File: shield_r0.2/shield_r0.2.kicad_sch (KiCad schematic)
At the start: 10 parts, among them X6 X6, X7 X7, X8 X8, X9 X9

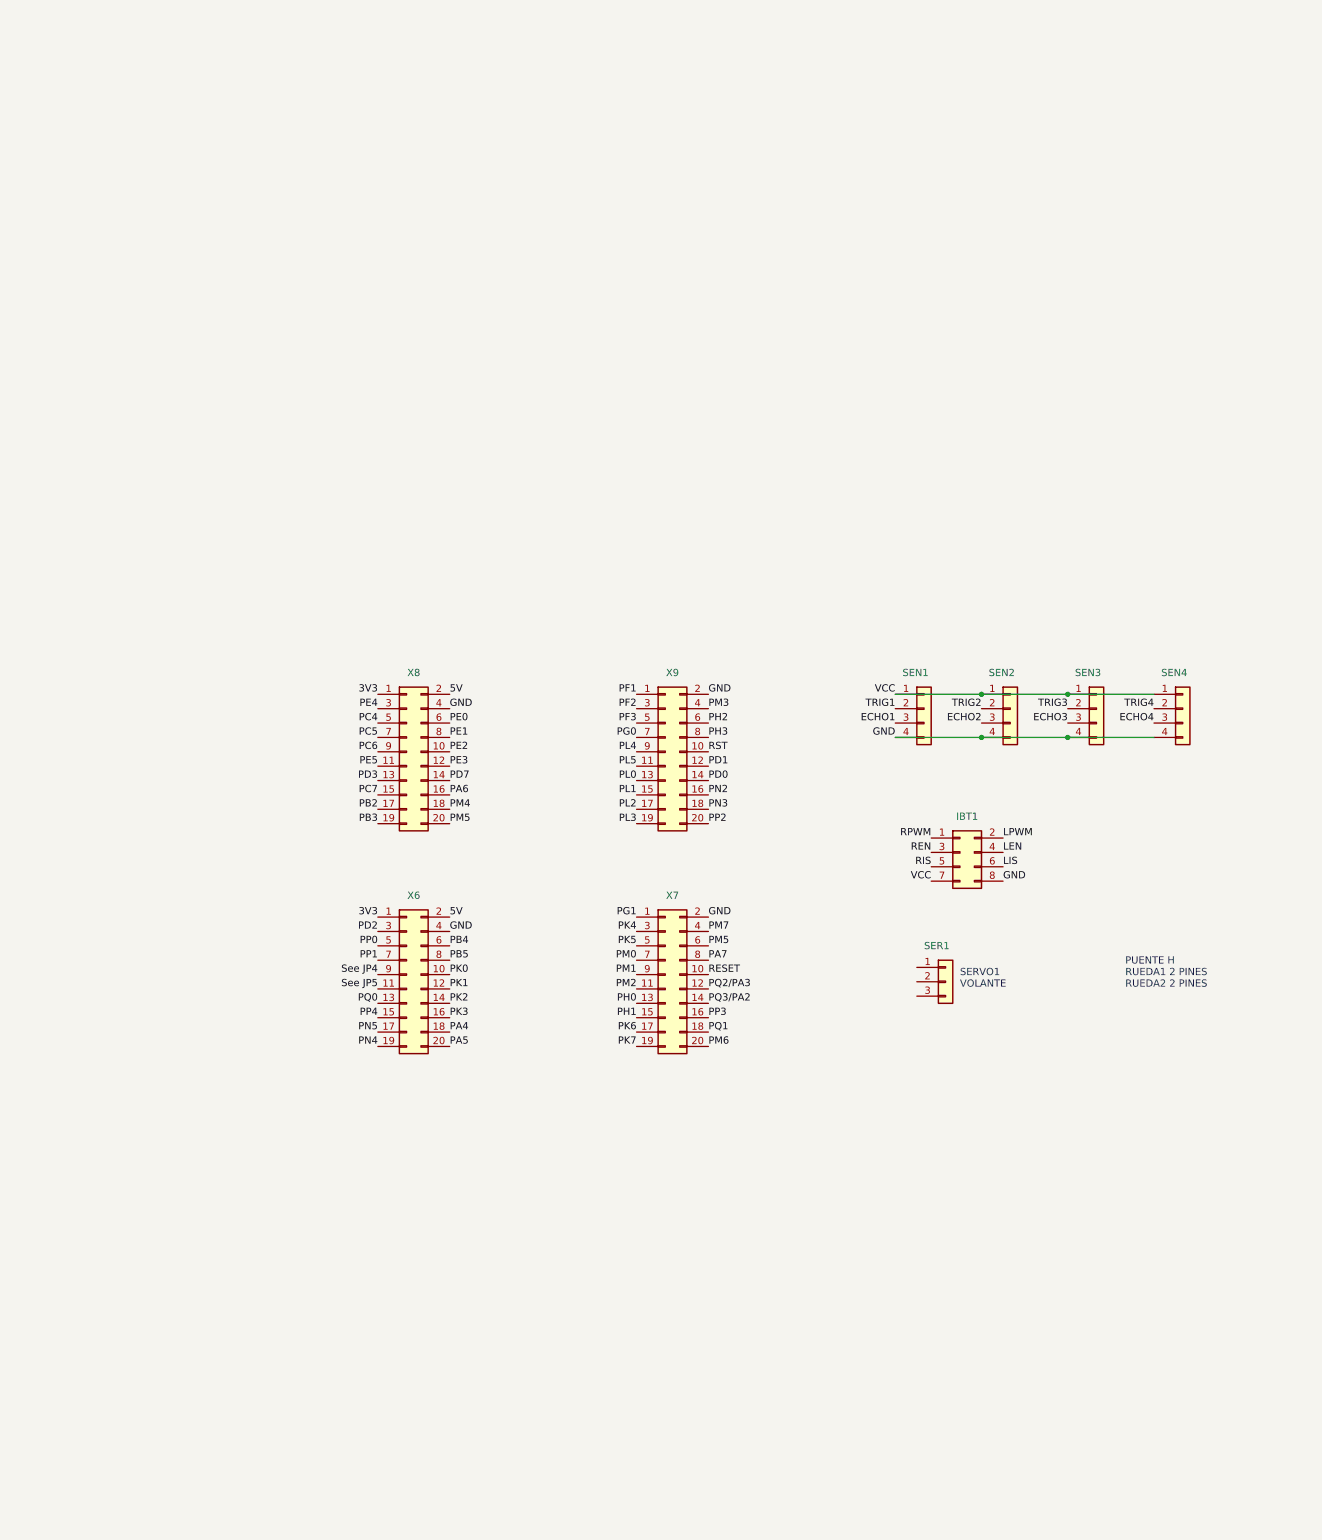
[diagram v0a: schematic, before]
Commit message: crear librerías ibt-2 y tiva-c, muestra shield
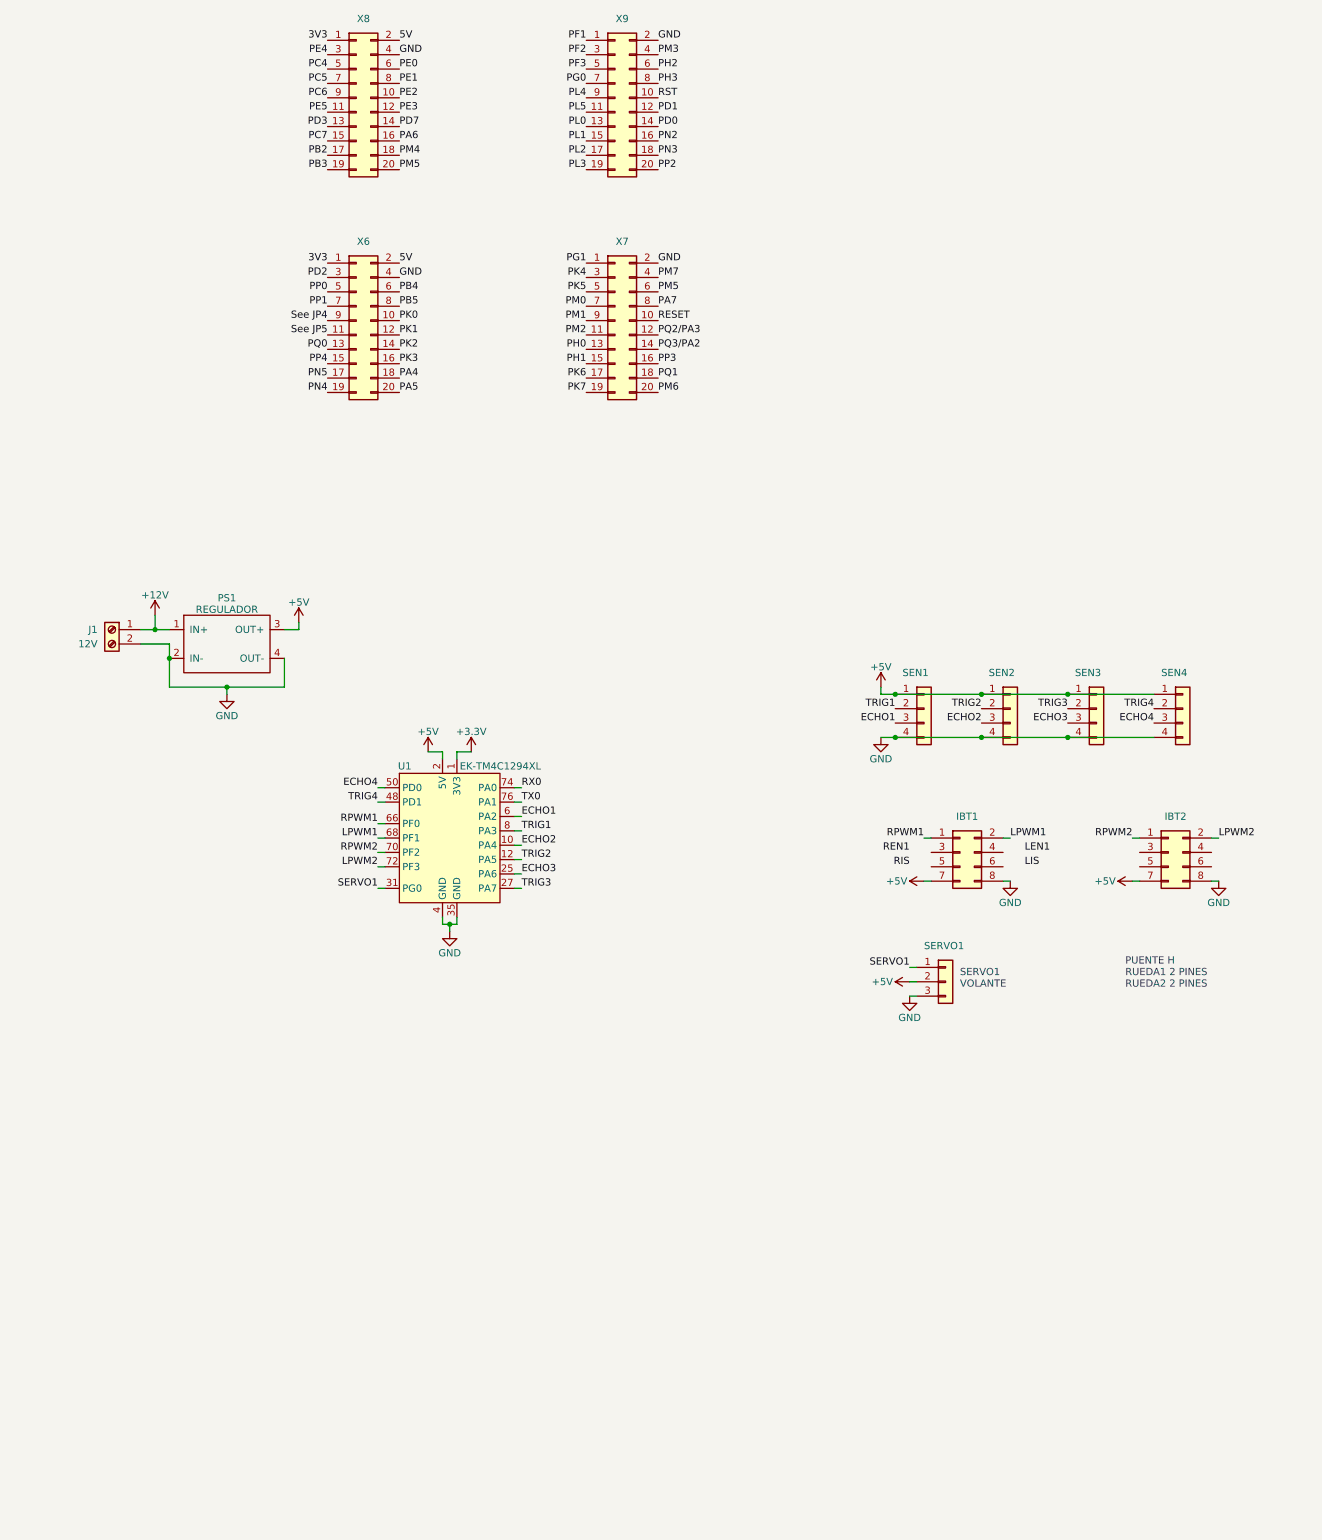
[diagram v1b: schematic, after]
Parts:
- added IBT2: Conn_02x04_Odd_Even, LaunchPad:IBT_2-01, symbol Connector_Generic:Conn_02x04_Odd_Even
- added J1: 12V, TerminalBlock:TerminalBlock_bornier-2_P5.08mm, symbol Connector:Screw_Terminal_01x02
- added PS1: REGULADOR, XL4005:XL4005_DC-DC, symbol XL4005_DC-DC:XL4005_DC-DC
- added U1: EK-TM4C1294XL, LaunchPad:EK-TM4C1294XL-01, symbol LaunchPad:EK-TM4C1294XL-01
- IBT1: footprint Connector_PinHeader_2.54mm:PinHeader_2x04_P2.54mm_Vertical -> LaunchPad:IBT_2-01
- renumbered SER1 to SERVO1
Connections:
- net VCC is gone; now on net +5V: IBT1.7 (Pin_7), SEN1.1 (Pin_1), SEN2.1 (Pin_1), SEN3.1 (Pin_1), SEN4.1 (Pin_1)
- net ECHO1: now also U1.6 (PA2)
- net ECHO2: now also U1.10 (PA4)
- net ECHO3: now also U1.25 (PA6)
- net ECHO4: now also U1.50 (PD0)
- net GND: now also SERVO1.3 (Pin_3), IBT2.8 (Pin_8), J1.2 (Pin_2), PS1.2 (IN-), PS1.4 (OUT-), U1.35 (GND), U1.4 (GND)
- net LIS: no longer IBT1.6 (Pin_6)
- net RIS: no longer IBT1.5 (Pin_5)
- net TRIG1: now also U1.8 (PA3)
- net TRIG2: now also U1.12 (PA5)
- net TRIG3: now also U1.27 (PA7)
- net TRIG4: now also U1.48 (PD1)
- net SERVO1: now reaches SERVO1.1 (Pin_1)
- net SERVO1: now also U1.31 (PG0)
- net +5V: now reaches SERVO1.2 (Pin_2)
- net +5V: now also IBT2.7 (Pin_7), PS1.3 (OUT+), U1.2 (5V)
- net LEN: no longer names the net of IBT1.4 (Pin_4)
- net LPWM renamed LPWM1
- net LPWM1: now also U1.68 (PF1)
- net REN: no longer names the net of IBT1.3 (Pin_3)
- net RPWM renamed RPWM1
- net RPWM1: now also U1.66 (PF0)
- new net +12V: J1.1 (Pin_1), PS1.1 (IN+)
- new net +3.3V: U1.1 (3V3)
- new net LPWM2: IBT2.2 (Pin_2), U1.72 (PF3)
- new net RPWM2: IBT2.1 (Pin_1), U1.70 (PF2)
- new net RX0: U1.74 (PA0)
- new net TX0: U1.76 (PA1)
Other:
- moved on the sheet: X6, X7, X8, X9

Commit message: conector bluetooth
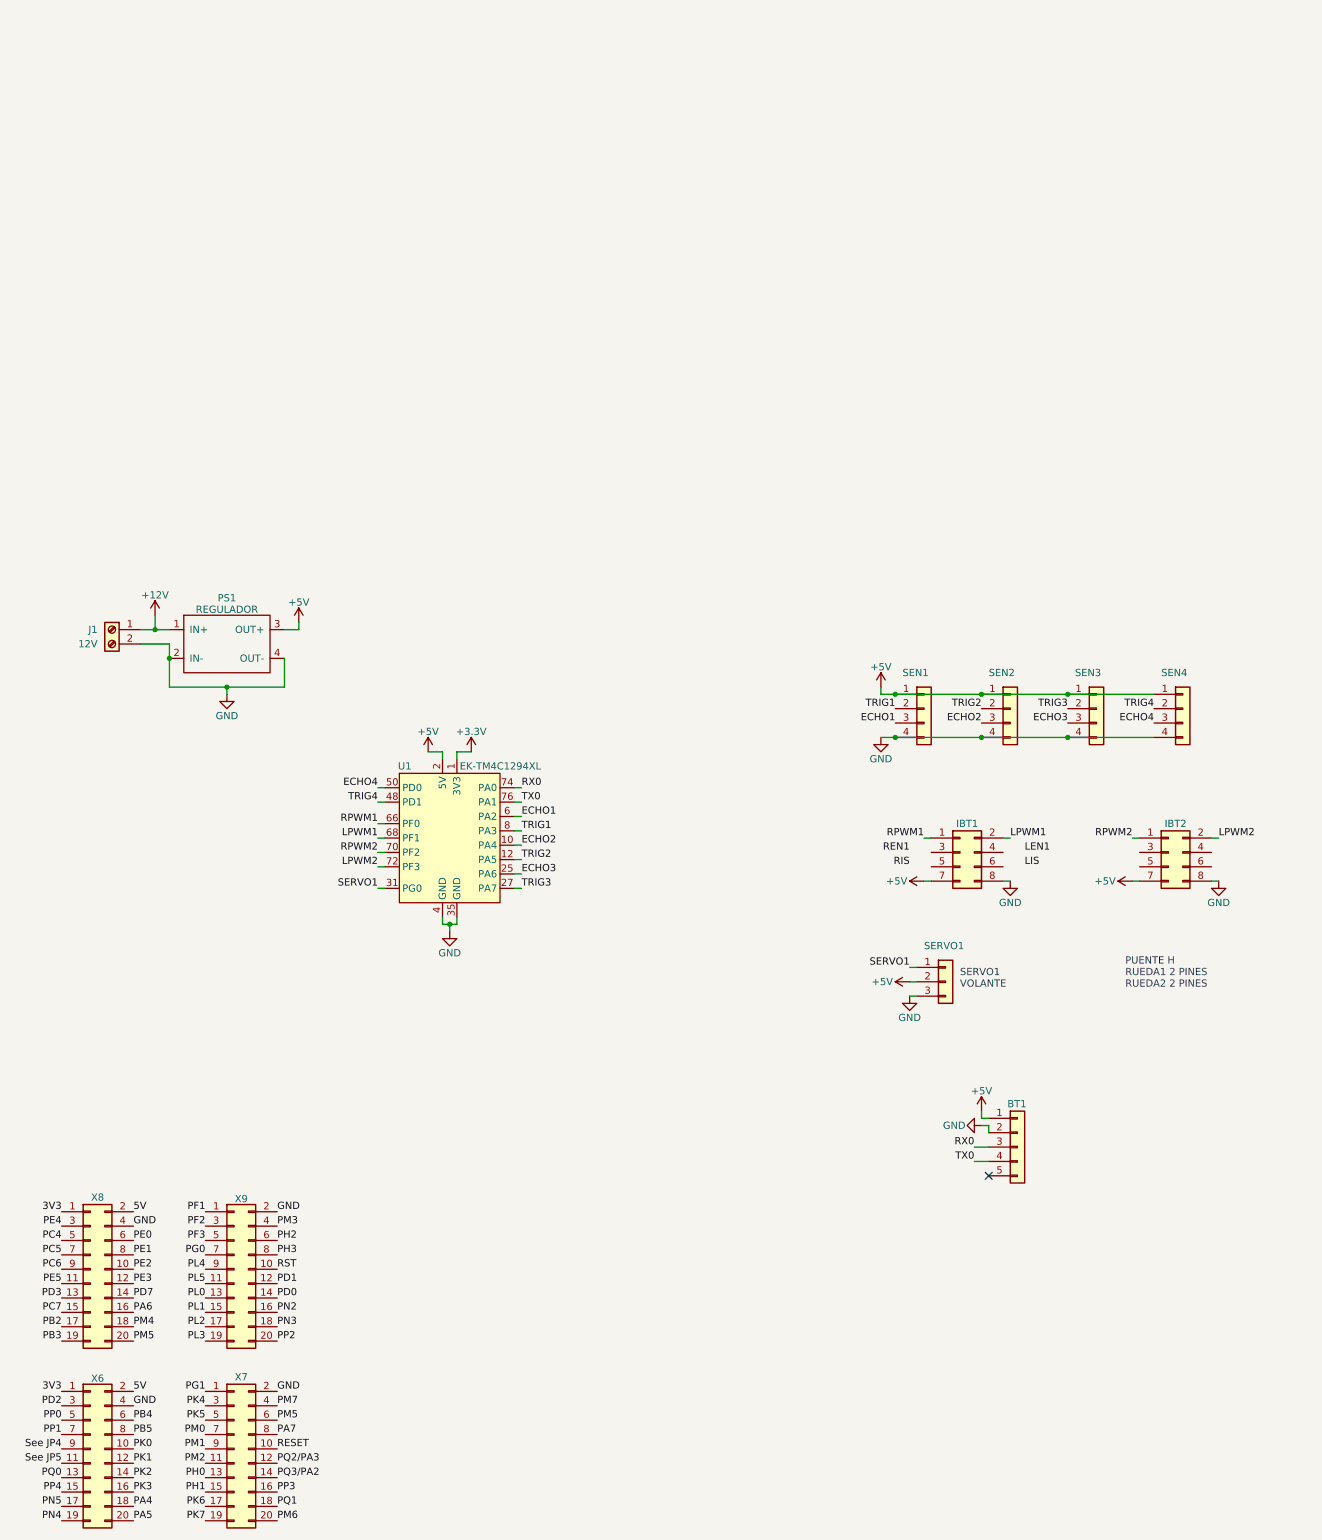
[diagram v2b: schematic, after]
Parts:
- added BT1: Conn_01x05, Connector_PinHeader_2.54mm:PinHeader_1x05_P2.54mm_Vertical, symbol Connector_Generic:Conn_01x05
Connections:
- net +5V: now also BT1.1 (Pin_1)
- net GND: now also BT1.2 (Pin_2)
- net RX0: now also BT1.3 (Pin_3)
- net TX0: now also BT1.4 (Pin_4)
- no-connect marks 0 -> 1
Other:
- moved on the sheet: X6, X7, X8, X9

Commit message: shield para fabricar
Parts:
- J1: footprint TerminalBlock:TerminalBlock_bornier-2_P5.08mm -> Connector_Molex:Molex_KK-254_AE-6410-02A_1x02_P2.54mm_Vertical
- PS1: footprint XL4005:XL4005_DC-DC -> Connector_PinHeader_2.54mm:PinHeader_2x02_P2.54mm_Vertical
- X6, X7, X8, X9: footprint Connector_PinHeader_2.54mm:PinHeader_2x10_P2.54mm_Vertical -> (none)
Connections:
- net +5V: now also IBT1.3 (Pin_3), IBT1.4 (Pin_4), IBT2.3 (Pin_3), IBT2.4 (Pin_4)
- no-connect marks 1 -> 5
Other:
- note added: "L_EN"
- note added: "L_IS"
- note added: "R_EN"
- note added: "R_IS"
- note added: "módulo bluetooth"
- note added: "puente H"
- note added: "sensores ultrasónicos"
- note added: "servo1 volante"
- note removed: "PUENTE H RUEDA1 2 PINES RUEDA2 2 PINES"
- note removed: "SERVO1 VOLANTE"
- moved on the sheet: BT1, IBT1, IBT2, J1, PS1, SEN1, SEN2, SEN3, SEN4, SERVO1, U1
